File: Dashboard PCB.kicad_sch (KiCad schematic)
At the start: 21 parts, among them J1 CONTROLS_EXPORT_CABLE_02X08, J2 Power, J3 Lights, J4 Main_Drive, J5 Extra

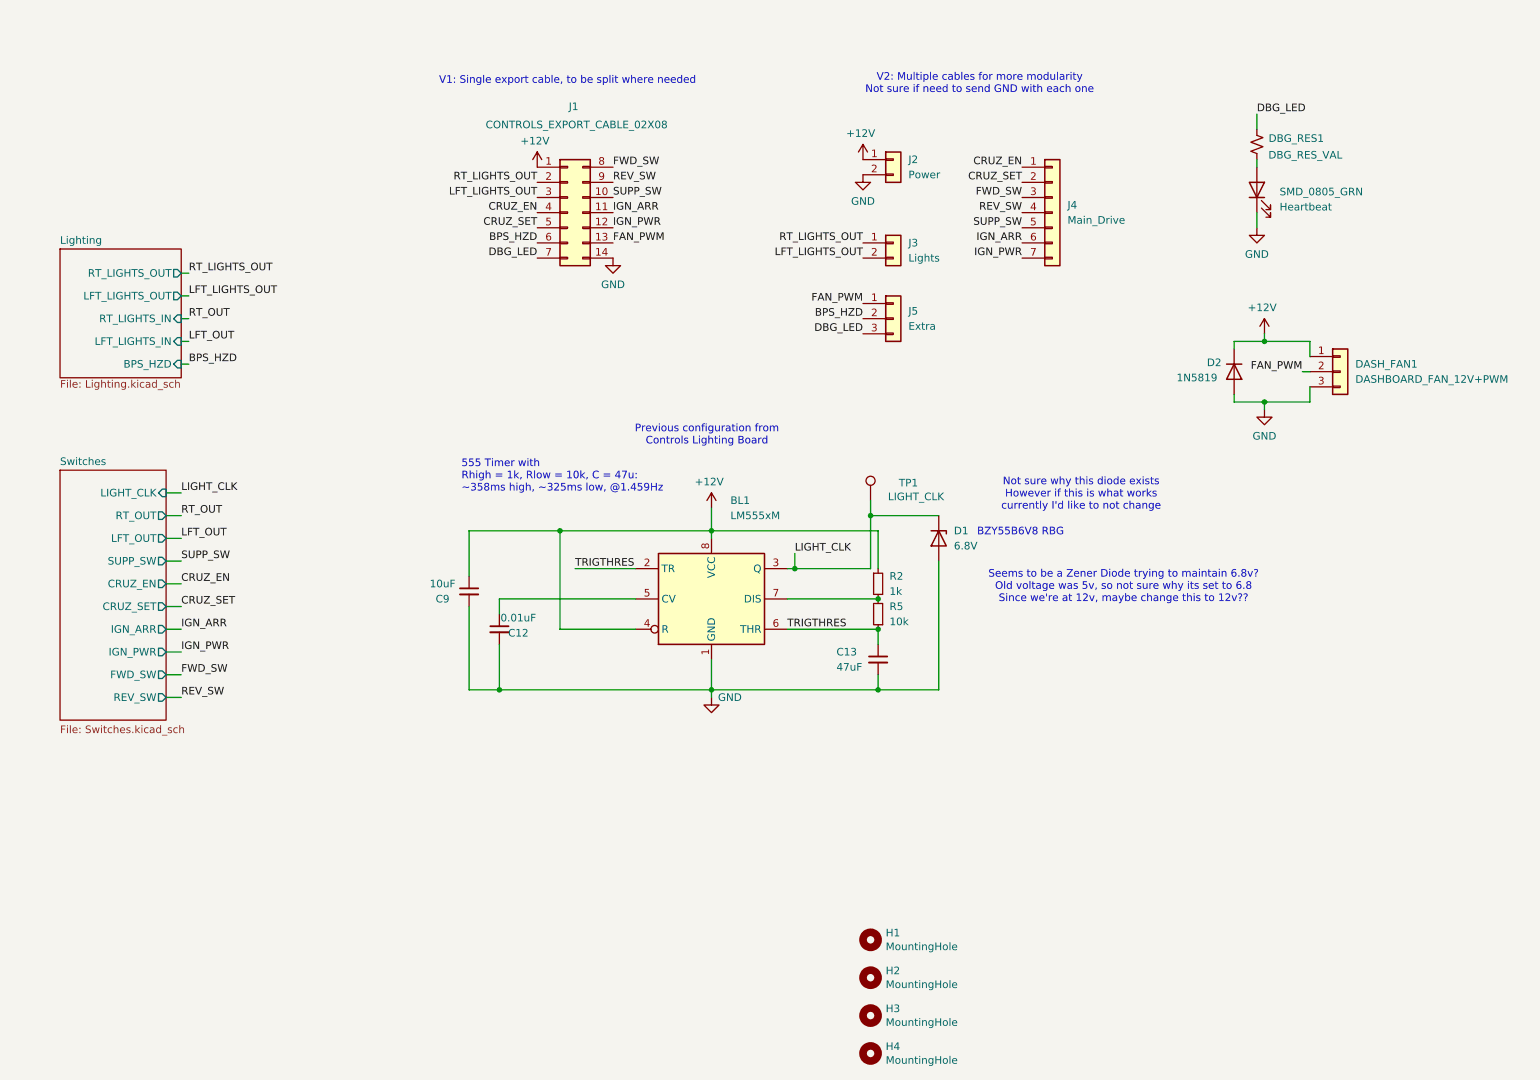
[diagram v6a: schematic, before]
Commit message: Ready for review
Controls decided to move a bunch of stuff back to leaderboard, also I think I fixed everything else.
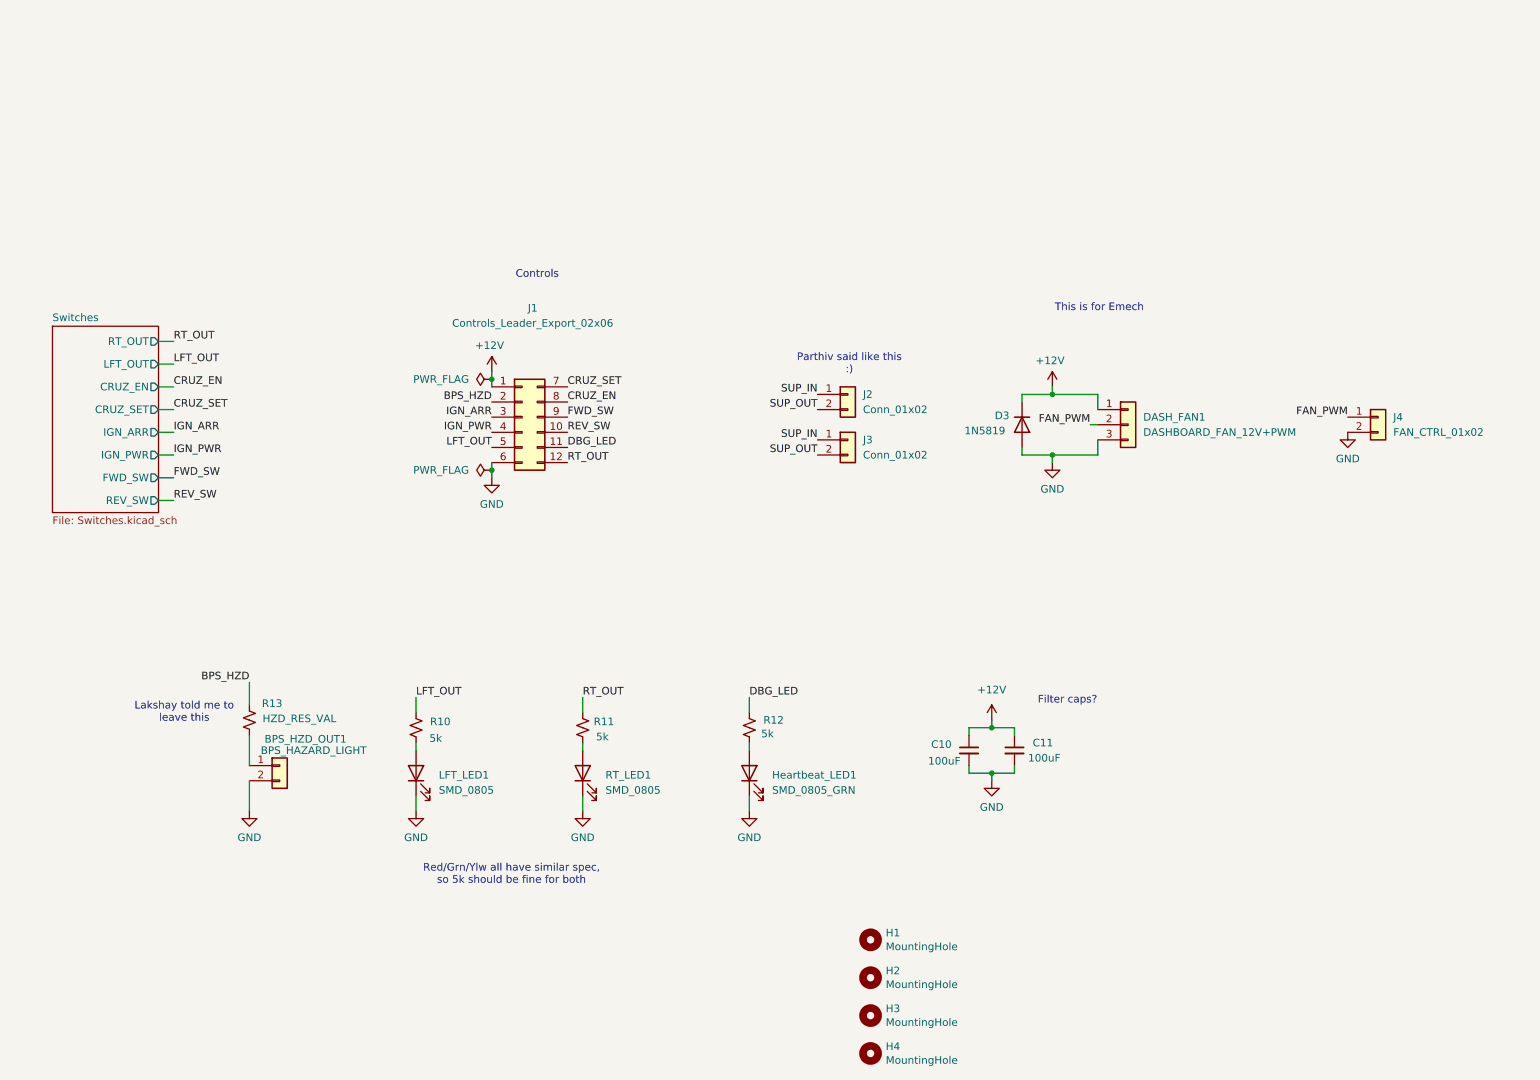
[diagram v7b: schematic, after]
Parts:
- removed BL1: LM555xM, Package_SO:SOIC-8_3.9x4.9mm_P1.27mm, symbol Timer:LM555xM
- removed C12: 0.01uF, Capacitor_SMD:C_0805_2012Metric, symbol Device:C_Small
- removed C13: 47uF, Capacitor_SMD:C_0805_2012Metric, symbol Device:C_Small
- removed C9: 10uF, Capacitor_SMD:C_0805_2012Metric, symbol Device:C_Small
- removed D1: 6.8V, Diode_SMD:D_0805_2012Metric, symbol Device:D_Zener
- removed J1: CONTROLS_EXPORT_CABLE_02X08, symbol Connector_Generic:Conn_02x07_Top_Bottom
- removed J4: Main_Drive, symbol Connector_Generic:Conn_01x07
- removed J5: Extra, symbol Connector_Generic:Conn_01x03
- removed R2: 1k, Resistor_SMD:R_0805_2012Metric, symbol Device:R_Small
- removed R5: 10k, Resistor_SMD:R_0805_2012Metric, symbol Device:R_Small
- removed TP1: LIGHT_CLK, TestPoint:TestPoint_Pad_1.5x1.5mm, symbol Connector:TestPoint
- added BPS_HZD_OUT1: BPS_HAZARD_LIGHT, Connector_Molex:Molex_Micro-Fit_3.0_43650-0215_1x02_P3.00mm_Vertical, symbol Connector_Generic:Conn_01x02
- added C10, C11: 100uF, Capacitor_SMD:C_0805_2012Metric, symbol Device:C_Small
- added J1: Controls_Leader_Export_02x06, symbol Connector_Generic:Conn_02x06_Top_Bottom
- added J4: FAN_CTRL_01x02, symbol Connector_Generic:Conn_01x02
- added LFT_LED1, RT_LED1: SMD_0805, symbol Device:LED
- added R10, R11: 5k, Resistor_SMD:R_0805_2012Metric, symbol Device:R_Small_US
- added R13: HZD_RES_VAL, Resistor_SMD:R_0805_2012Metric, symbol Device:R_Small_US
- Heartbeat_LED1: renamed from SMD_0805_GRN; value Heartbeat -> SMD_0805_GRN
- J2: value Power -> Conn_01x02
- J3: value Lights -> Conn_01x02
- R12: renamed from DBG_RES1; value DBG_RES_VAL -> 5k
- renumbered D2 to D3
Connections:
- net +12V: now also C10.1, C11.1, J1.1 (Pin_1); no longer J2.1 (Pin_1)
- net BPS_HZD: now also J1.2 (Pin_2), R13.1
- net CRUZ_EN: now also J1.8 (Pin_8)
- net CRUZ_SET: now also J1.7 (Pin_7)
- net DBG_LED: now also J1.11 (Pin_11)
- net FAN_PWM: now also J4.1 (Pin_1)
- net FWD_SW: now also J1.9 (Pin_9)
- net GND: now also BPS_HZD_OUT1.2 (Pin_2), C10.2, C11.2, J1.6 (Pin_6), J4.2 (Pin_2), LFT_LED1.1 (K), RT_LED1.1 (K); no longer J2.2 (Pin_2)
- net IGN_ARR: now also J1.3 (Pin_3)
- net IGN_PWR: now also J1.4 (Pin_4)
- net LFT_OUT: now also J1.5 (Pin_5), R10.1
- net REV_SW: now also J1.10 (Pin_10)
- net RT_OUT: now also J1.12 (Pin_12), R11.1
- net LFT_LIGHTS_OUT renamed SUP_OUT
- net SUP_OUT: now also J2.2 (Pin_2)
- net RT_LIGHTS_OUT renamed SUP_IN
- net SUP_IN: now also J2.1 (Pin_1)
- new net: R11.2, RT_LED1.2 (A)
- new net: LFT_LED1.2 (A), R10.2
- new net: BPS_HZD_OUT1.1 (Pin_1), R13.2
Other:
- removed sheet Lighting
- sheet Switches ports: added none; removed LIGHT_CLK, SUPP_SW
- note added: "Controls"
- note added: "Filter caps?"
- note added: "Lakshay told me to leave this"
- note added: "Parthiv said like this :)"
- note added: "Red/Grn/Ylw all have similar spec, so 5k should be fine for both"
- note added: "This is for Emech"
- note removed: "555 Timer with Rhigh = 1k, Rlow = 10k, C = 47u: ~358ms high, ~325ms low, @1.459Hz"
- note removed: "BZY55B6V8 RBG"
- note removed: "Not sure why this diode exists However if this is what works currently I'd like to not change"
- note removed: "Previous configuration from Controls Lighting Board"
- note removed: "Seems to be a Zener Diode trying to maintain 6.8v? Old voltage was 5v, so not sure why its set to 6.8 Since we're at 12v, maybe change this to 12v??"
- note removed: "V1: Single export cable, to be split where needed"
- note removed: "V2: Multiple cables for more modularity Not sure if need to send GND with each one"
- moved on the sheet: D3, DASH_FAN1, Heartbeat_LED1, R12

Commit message: Made pretty
Fixed a few things up and made it pretty.
Still need to double check a few things and assign all footprints
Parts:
- added +12V1, CRUZ_EN1, CRUZ_SET1, DBG_LED1, FAN_PWM1, FWD_SW1, GND1, IGN_ARR1, IGN_PWR1, LFT_OUT1, REV_SW1, RT_OUT1: TestPoint, symbol Connector:TestPoint
- R10, R11, R12: value 5k -> 5.1k
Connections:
- net +12V: now also +12V1.1
- net CRUZ_EN: now also CRUZ_EN1.1
- net CRUZ_SET: now also CRUZ_SET1.1
- net DBG_LED: now also DBG_LED1.1
- net FAN_PWM: now also FAN_PWM1.1
- net FWD_SW: now also FWD_SW1.1
- net GND: now also GND1.1
- net IGN_ARR: now also IGN_ARR1.1
- net IGN_PWR: now also IGN_PWR1.1
- net LFT_OUT: now also LFT_OUT1.1
- net REV_SW: now also REV_SW1.1
- net RT_OUT: now also RT_OUT1.1
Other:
- note added: "BPS Hazard light is seperate from board. Resistor may not be needed, it's here in case."
- note added: "Check datasheet of "DASH_FAN1" for extra info"
- note added: "Controls Export Connection"
- note added: "Dashboard Fan"
- note added: "Due to supplemental switch being in parralel with battery, this is only for a place to solder the switch down. The connection will be seperate from the board"
- note added: "Fan control being sent into board"
- note added: "Filter Caps :P"
- note added: "LED!"
- note added: "LEDs will be constant"
- note added: "Note: All logic is 12V"
- note added: "Supplemental Battery Switch Solder Holes (No connection to board)"
- note added: "Test Points >:("
- note removed: "Controls"
- note removed: "Filter caps?"
- note removed: "Lakshay told me to leave this"
- note removed: "Parthiv said like this :)"
- note removed: "Red/Grn/Ylw all have similar spec, so 5k should be fine for both"
- note removed: "This is for Emech"
- moved on the sheet: BPS_HZD_OUT1, C10, C11, D3, DASH_FAN1, Heartbeat_LED1, J1, J2, J3, J4, LFT_LED1, R10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
